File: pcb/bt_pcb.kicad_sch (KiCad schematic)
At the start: 29 parts, among them IC4 STM32H750VBT6, IC5 W25Q512JVEIM, J12 USB_C_Receptacle, J2 Conn_JTAG_SWD_10, J4 Conn_01x10, Y1 Crystal

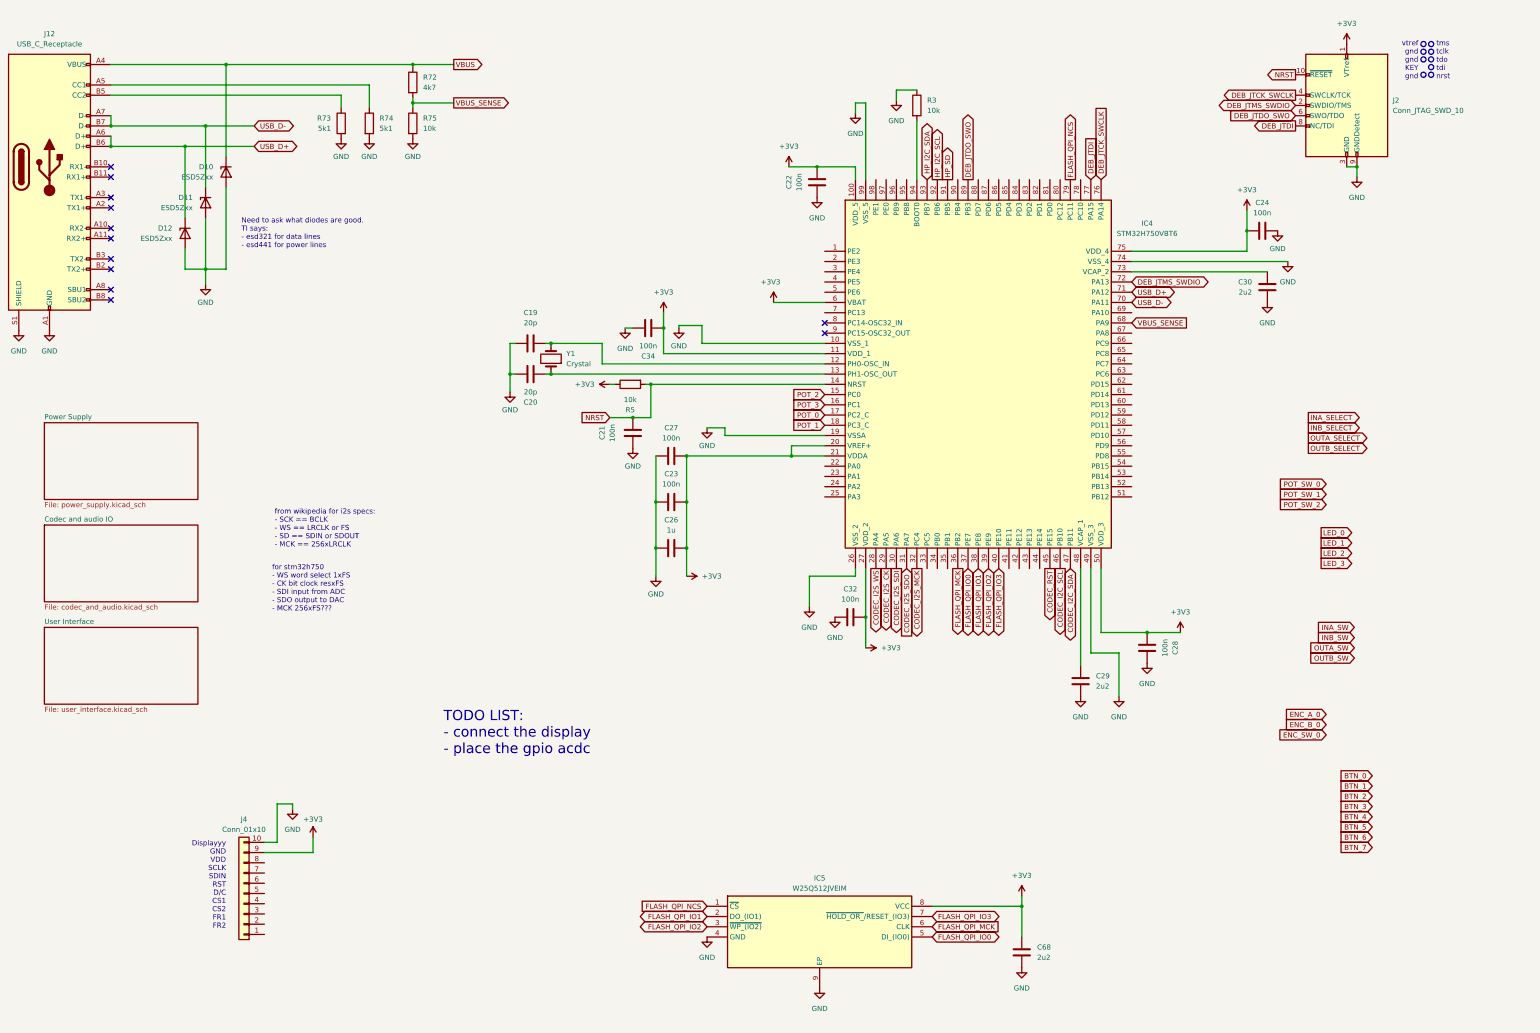
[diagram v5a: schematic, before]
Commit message: schematic finished, now under revision
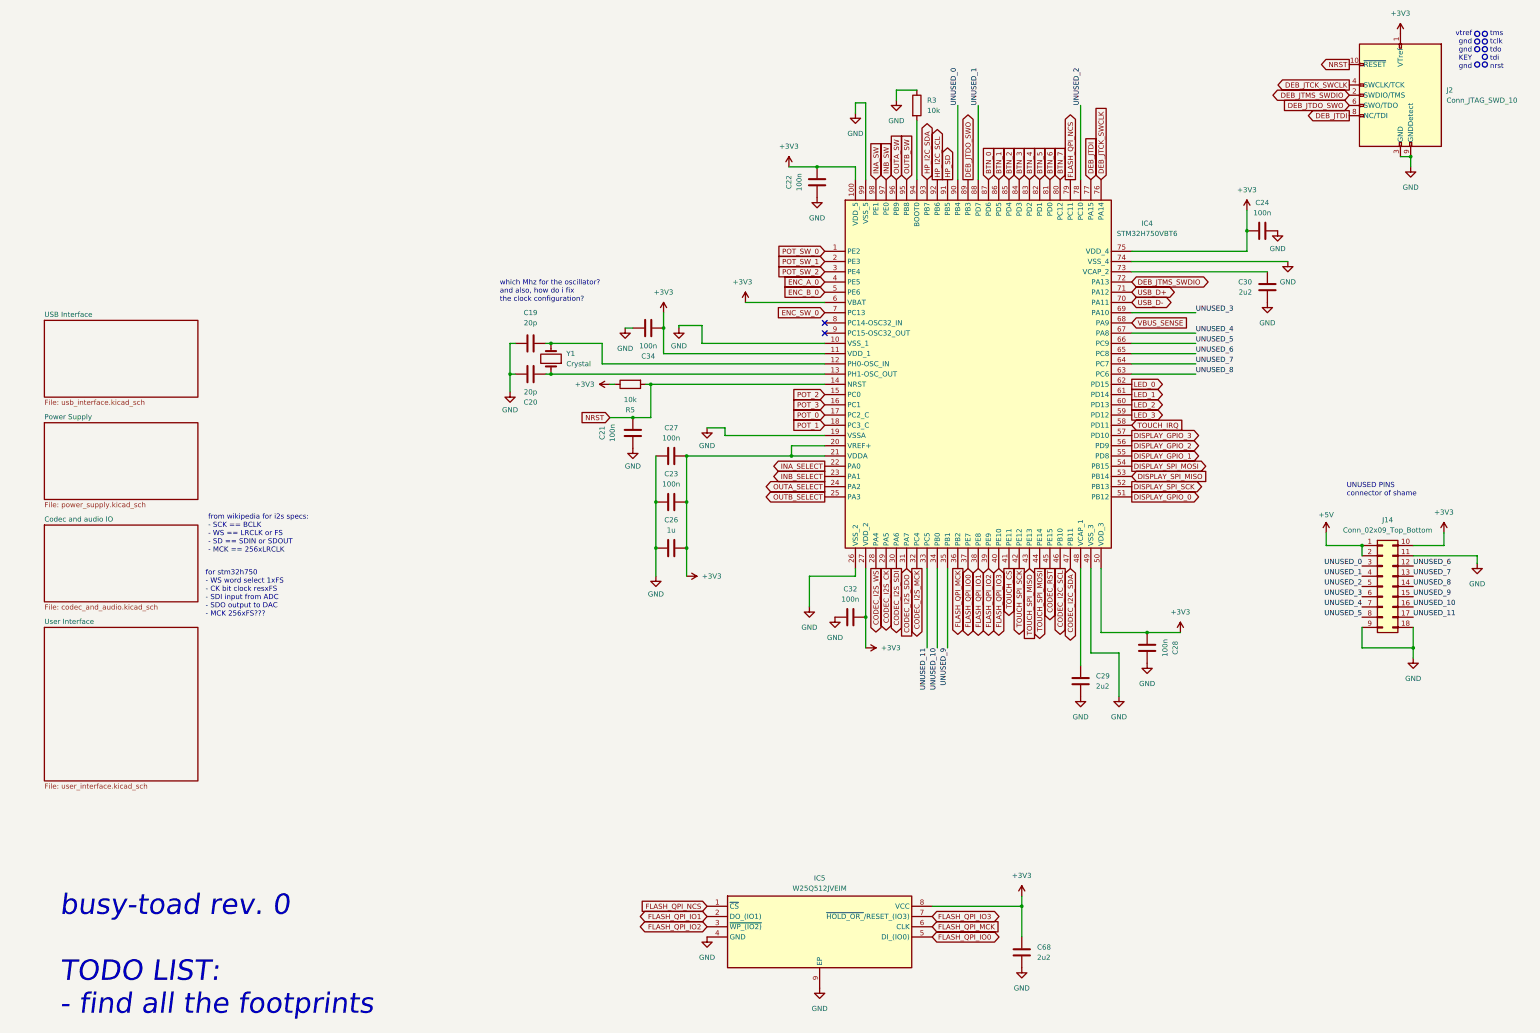
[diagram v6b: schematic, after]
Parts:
- removed D10, D11, D12: ESD5Zxx, Diode_SMD:D_SOD-523, symbol Diode:ESD5Zxx
- removed J12: USB_C_Receptacle, symbol Connector:USB_C_Receptacle
- removed J4: Conn_01x10, symbol Connector_Generic:Conn_01x10
- removed R72: 4k7, symbol Device:R
- removed R73, R74: 5k1, symbol Device:R
- removed R75: 10k, symbol Device:R
- added J14: Conn_02x09_Top_Bottom, symbol Connector_Generic:Conn_02x09_Top_Bottom
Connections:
- net +3V3: now also J14.10 (Pin_10)
- net BTN_0: now also IC4.87 (PD6)
- net BTN_1: now also IC4.86 (PD5)
- net BTN_2: now also IC4.85 (PD4)
- net BTN_3: now also IC4.84 (PD3)
- net BTN_4: now also IC4.83 (PD2)
- net BTN_5: now also IC4.82 (PD1)
- net BTN_6: now also IC4.81 (PD0)
- net BTN_7: now also IC4.80 (PC12)
- net ENC_A_0: now also IC4.4 (PE5)
- net ENC_B_0: now also IC4.5 (PE6)
- net ENC_SW_0: now also IC4.7 (PC13)
- net GND: now also J14.11 (Pin_11), J14.18 (Pin_18), J14.9 (Pin_9)
- net INA_SELECT: now also IC4.22 (PA0)
- net INA_SW: now also IC4.98 (PE1)
- net INB_SELECT: now also IC4.23 (PA1)
- net INB_SW: now also IC4.97 (PE0)
- net LED_0: now also IC4.62 (PD15)
- net LED_1: now also IC4.61 (PD14)
- net LED_2: now also IC4.60 (PD13)
- net LED_3: now also IC4.59 (PD12)
- net OUTA_SELECT: now also IC4.24 (PA2)
- net OUTA_SW: now also IC4.96 (PB9)
- net OUTB_SELECT: now also IC4.25 (PA3)
- net OUTB_SW: now also IC4.95 (PB8)
- net POT_SW_0: now also IC4.1 (PE2)
- net POT_SW_1: now also IC4.2 (PE3)
- net POT_SW_2: now also IC4.3 (PE4)
- net UNUSED_11: now reaches IC4.33 (PC5)
- net UNUSED_11: now also J14.17 (Pin_17)
- net UNUSED_10: now reaches IC4.34 (PB0)
- net UNUSED_10: now also J14.16 (Pin_16)
- net UNUSED_9: now reaches IC4.35 (PB1)
- net UNUSED_9: now also J14.15 (Pin_15)
- net TOUCH_CS: now reaches IC4.41 (PE11)
- net TOUCH_SPI_SCK: now reaches IC4.42 (PE12)
- net TOUCH_SPI_MISO: now reaches IC4.43 (PE13)
- net TOUCH_SPI_MOSI: now reaches IC4.44 (PE14)
- net DISPLAY_GPIO_0: now reaches IC4.51 (PB12)
- net DISPLAY_SPI_SCK: now reaches IC4.52 (PB13)
- net DISPLAY_SPI_MISO: now reaches IC4.53 (PB14)
- net DISPLAY_SPI_MOSI: now reaches IC4.54 (PB15)
- net DISPLAY_GPIO_1: now reaches IC4.55 (PD8)
- net DISPLAY_GPIO_2: now reaches IC4.56 (PD9)
- net DISPLAY_GPIO_3: now reaches IC4.57 (PD10)
- net TOUCH_IRQ: now reaches IC4.58 (PD11)
- net UNUSED_8: now reaches IC4.63 (PC6)
- net UNUSED_8: now also J14.14 (Pin_14)
- net UNUSED_7: now reaches IC4.64 (PC7)
- net UNUSED_7: now also J14.13 (Pin_13)
- net UNUSED_6: now reaches IC4.65 (PC8)
- net UNUSED_6: now also J14.12 (Pin_12)
- net UNUSED_5: now reaches IC4.66 (PC9)
- net UNUSED_5: now also J14.8 (Pin_8)
- net UNUSED_4: now reaches IC4.67 (PA8)
- net UNUSED_4: now also J14.7 (Pin_7)
- net UNUSED_3: now reaches IC4.69 (PA10)
- net UNUSED_3: now also J14.6 (Pin_6)
- net UNUSED_2: now reaches IC4.78 (PC10)
- net UNUSED_2: now also J14.5 (Pin_5)
- net UNUSED_1: now reaches IC4.88 (PD7)
- net UNUSED_1: now also J14.4 (Pin_4)
- net UNUSED_0: now reaches IC4.90 (PB4)
- net UNUSED_0: now also J14.3 (Pin_3)
- new net +5V: J14.1 (Pin_1), J14.2 (Pin_2)
- no-connect marks 12 -> 2
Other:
- added sheet USB Interface (usb_interface.kicad_sch)
- note added: "UNUSED PINS connector of shame"
- note added: "busy-toad rev. 0 TODO LIST: - find all the footprints"
- note added: "which Mhz for the oscillator? and also, how do i fix the clock configuration?"
- note removed: "Displayyy GND VDD SCLK SDIN RST D/C CS1 CS2 FR1 FR2"
- note removed: "Need to ask what diodes are good. TI says: - esd321 for data lines - esd441 for power lines"
- note removed: "TODO LIST: - connect the display - place the gpio acdc"
- moved on the sheet: J2

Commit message: starting the revision from ed
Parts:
- removed C19, C20: 20p, symbol Device:C
- removed C21, C22, C23, C24, C27, C28, C32, C34: 100n, symbol Device:C
- removed C26: 1u, symbol Device:C
- removed C29, C30, C68: 2u2, symbol Device:C
- removed IC4: STM32H750VBT6, QFP50P1600X1600X160-100N, symbol SamacSys_Parts:STM32H750VBT6
- removed IC5: W25Q512JVEIM, SON127P800X600X80-9N-D, symbol SamacSys_Parts:W25Q512JVEIM
- removed J14: Conn_02x09_Top_Bottom, symbol Connector_Generic:Conn_02x09_Top_Bottom
- removed J2: Conn_JTAG_SWD_10, symbol Connector:Conn_ARM_JTAG_SWD_10
- removed R3, R5: 10k, symbol Device:R
- removed Y1: Crystal, symbol Device:Crystal
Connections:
- no-connect marks 2 -> 0
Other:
- added sheet MCUs (mcus.kicad_sch)
- note added: "busy-toad rev. 0 TODO LIST: - configurare secondo MCU (senza connettivita') - riformattare passivi attorno MCUs - aggiungere ESD a input (audio e controlli) EVG's NOTES: - usare cs per spi (display e touch) - usare un mcu per grafica - cercare un altro schermo (dfrobot, dfr0665) - sistemare 9v->5v (anche un ldo, tma05120, adpl16000) - compattare audio analog - usare uno switch per cambiare modo d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"
- note removed: "UNUSED PINS connector of shame"
- note removed: "busy-toad rev. 0 TODO LIST: - find all the footprints"
- note removed: "tms tclk tdo tdi nrst"
- note removed: "vtref gnd gnd KEY gnd"
- note removed: "which Mhz for the oscillator? and also, how do i fix the clock configuration?"

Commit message: reprising work
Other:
- note added: "busy-toad TODO LIST: - configurare secondo MCU (senza connettivita') - riformattare passivi attorno MCUs - aggiungere ESD a input (audio e controlli) EVG's NOTES: - usare cs per spi (display e touch) - usare un mcu per grafica - cercare un altro schermo (dfrobot, dfr0665) - sistemare 9v->5v (anche un ldo, tma05120, adpl16000) - compattare audio analog - usare uno switch per cambiare modo di uso o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"
- note removed: "busy-toad rev. 0 TODO LIST: - configurare secondo MCU (senza connettivita') - riformattare passivi attorno MCUs - aggiungere ESD a input (audio e controlli) EVG's NOTES: - usare cs per spi (display e touch) - usare un mcu per grafica - cercare un altro schermo (dfrobot, dfr0665) - sistemare 9v->5v (anche un ldo, tma05120, adpl16000) - compattare audio analog - usare uno switch per cambiare modo d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"
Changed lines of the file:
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@@
 (kicad_sch (version 20230121) (generator eeschema)
   (paper "A4")
-  (text "busy-toad rev. 0\n\nTODO LIST:\n- configurare secondo MCU (senza connettivita')\n- riformattare passivi attorno MCUs\n- aggiungere ESD a input (audio e controlli)\n\nEVG's NOTES:\n- usare cs per spi (display e touch)\n- usare un mcu per grafica\n- cercare un altro schermo (dfrobot, dfr0665)\n- sistemare 9v->5v (anche un ldo, tma05120, adpl16000)\n- compattare audio analog\n  - usare uno switch per cambiare modo di uso opamp (adg611) \n  - usare uno switch per spegnere e accendere opamp\n  - cambiare switch perche' obsoleto\n"
+  (text "busy-toad\n\nTODO LIST:\n- configurare secondo MCU (senza connettivita')\n- riformattare passivi attorno MCUs\n- aggiungere ESD a input (audio e controlli)\n\nEVG's NOTES:\n- usare cs per spi (display e touch)\n- usare un mcu per grafica\n- cercare un altro schermo (dfrobot, dfr0665)\n- sistemare 9v->5v (anche un ldo, tma05120, adpl16000)\n- compattare audio analog\n  - usare uno switch per cambiare modo di uso opamp (adg611) \n  - usare uno switch per spegnere e accendere opamp\n  - cambiare switch perche' obsoleto\n"
     (at 115.57 145.415 0)
     (effects (font (size 2.54 2.54) italic) (justify left bottom))
